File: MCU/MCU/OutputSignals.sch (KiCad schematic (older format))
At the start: 31 parts, among them J11 Conn_01x02, J12 Conn_01x02, J13 Conn_01x02, Q2 8050, Q3 8050, Q4 8550, Q5 8050, U10 LMV321, U11 PC817, U9 ICL7660

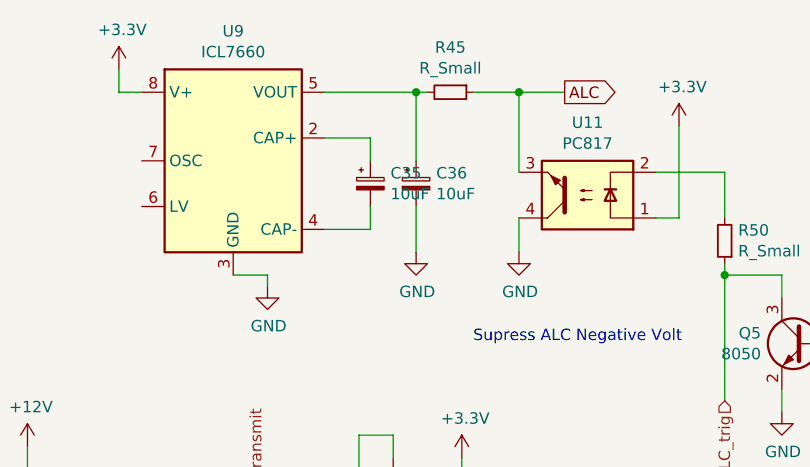
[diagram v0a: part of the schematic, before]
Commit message: MCU routed
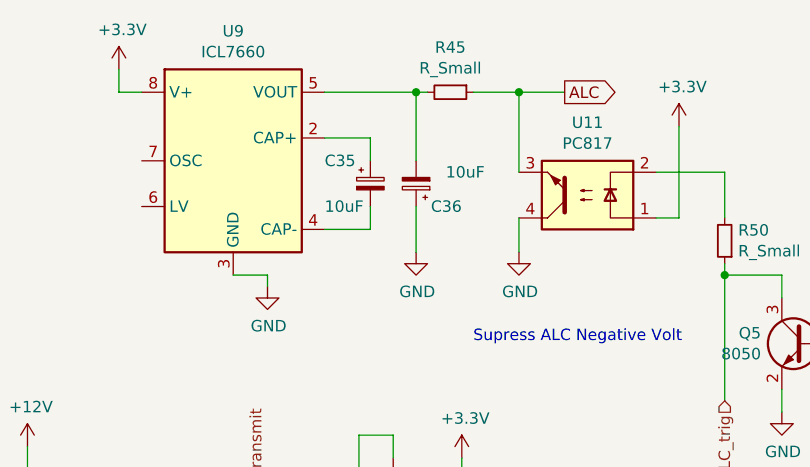
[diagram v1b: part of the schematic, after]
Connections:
- net GND: now also C36.1; no longer C36.2
- net at R45.2, U9.5 (VOUT): now also C36.2; no longer C36.1
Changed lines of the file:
@@
 U 1 1 5E7F3AB6
 P 3350 1500
-F 0 "C35" H 3438 1546 50  0000 L CNN
-F 1 "10uF" H 3438 1455 50  0000 L CNN
+F 0 "C35" H 3150 1600 50  0000 L CNN
+F 1 "10uF" H 3150 1400 50  0000 L CNN
 F 2 "Capacitors_SMD:C_0805" H 3350 1500 50  0001 C CNN
 F 3 "~" H 3350 1500 50  0001 C CNN
@@
 U 1 1 5E7F8AB0
 P 3550 1500
-F 0 "C36" H 3638 1546 50  0000 L CNN
-F 1 "10uF" H 3638 1455 50  0000 L CNN
+F 0 "C36" H 3350 1600 50  0000 L CNN
+F 1 "10uF" H 3250 1450 50  0000 L CNN
 F 2 "Capacitors_SMD:C_0805" H 3550 1500 50  0001 C CNN
 F 3 "~" H 3550 1500 50  0001 C CNN
 	1    3550 1500
-	1    0    0    -1
+	-1   0    0    1
 $EndComp
 Wire Wire Line
